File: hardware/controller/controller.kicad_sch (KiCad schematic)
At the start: 26 parts, among them J1 Conn_02x15_Odd_Even, J10 conn_wifi, J11 conn_gpio, J2 Conn_01x20, J3 Conn_01x20, J4 Conn_01x02, J5 conn_vol, J6 conn_bl, J7 conn_br, J8 conn_dsp, J9 conn_i2s_mplx, SW1 RESET, U1 Display_5"_RA8875, U2 TSR_1-2433, U3 TSR_1-2433, U5 TSR_1-2433

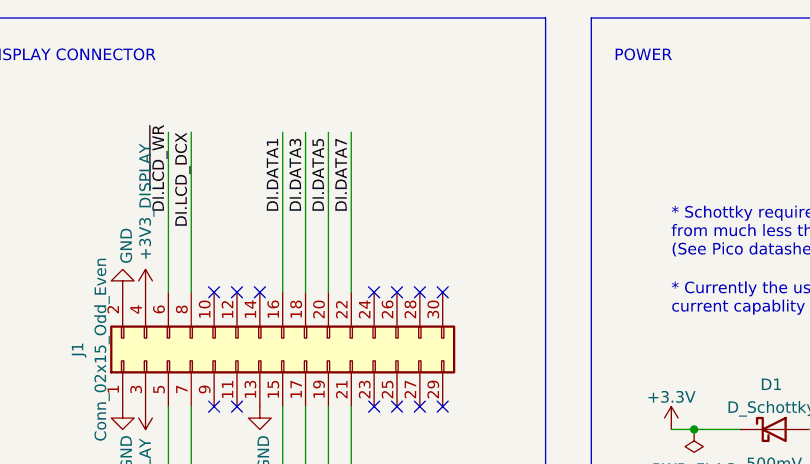
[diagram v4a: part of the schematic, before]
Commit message: Added (temp) backlight control
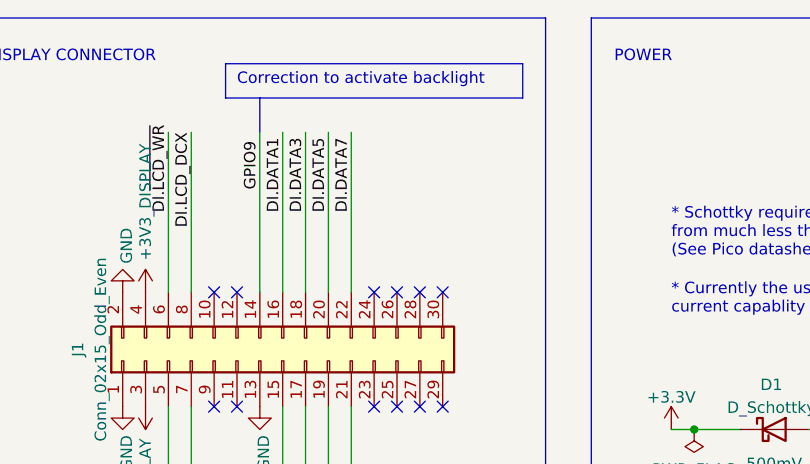
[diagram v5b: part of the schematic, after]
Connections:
- net GPIO9: now also J1.14 (Pin_14)
- no-connect marks 37 -> 36
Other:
- note added: "Correction to activate backlight"
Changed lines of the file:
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@@
   (no_connect (at 100.33 203.2))
   (no_connect (at 100.33 205.74))
-  (no_connect (at 148.59 46.99))
   (no_connect (at 143.51 46.99))
   (no_connect (at 64.77 166.37))
@@
     (stroke (width 0) (type default) (color 0 0 0 0))
   )
+  (polyline (pts (xy 148.59 25.4) (xy 148.59 29.21))
+    (stroke (width 0) (type default) (color 255 0 0 1))
+  )
   (wire (pts (xy 158.75 46.99) (xy 158.75 29.21))
     (stroke (width 0) (type default) (color 0 0 0 0))
@@
     (stroke (width 0) (type default) (color 0 0 0 0))
   )
+  (polyline (pts (xy 144.78 25.4) (xy 177.8 25.4))
+    (stroke (width 0) (type default) (color 255 0 0 1))
+  )
   (polyline (pts (xy 185.42 152.4) (xy 297.18 152.4))
     (stroke (width 0) (type default) (color 0 0 0 0))
@@
     (stroke (width 0) (type default) (color 0 0 0 0))
   )
+  (polyline (pts (xy 177.8 25.4) (xy 177.8 21.59))
+    (stroke (width 0) (type default) (color 255 0 0 1))
+  )
   (wire (pts (xy 345.44 229.87) (xy 345.44 231.14))
     (stroke (width 0) (type default) (color 0 0 0 0))
@@
     (stroke (width 0) (type default) (color 0 0 0 0))
   )
+  (polyline (pts (xy 144.78 21.59) (xy 177.8 21.59))
+    (stroke (width 0) (type default) (color 255 0 0 1))
+  )
   (wire (pts (xy 250.19 134.62) (xy 232.41 134.62))
     (stroke (width 0) (type default) (color 0 0 0 0))
@@
   (wire (pts (xy 317.5 87.63) (xy 346.71 87.63))
     (stroke (width 0) (type default) (color 0 0 0 0))
+  )
+  (polyline (pts (xy 144.78 21.59) (xy 144.78 25.4))
+    (stroke (width 0) (type default) (color 255 0 0 1))
   )
   (polyline (pts (xy 73.66 128.27) (xy 73.66 124.46))
@@
     (stroke (width 0) (type default) (color 0 0 0 0))
   )
+  (wire (pts (xy 148.59 29.21) (xy 148.59 46.99))
+    (stroke (width 0) (type default) (color 0 0 0 0))
+  )
   (wire (pts (xy 67.31 220.98) (xy 67.31 233.68))
     (stroke (width 0) (type default) (color 0 0 0 0))
@@
   )
   (text "Only 8 bit bus used" (at 63.5 88.9 0)
+    (effects (font (size 1.27 1.27)) (justify left bottom))
+  )
+  (text "Correction to activate backlight" (at 146.05 24.13 0)
     (effects (font (size 1.27 1.27)) (justify left bottom))
   )
@@
     (effects (font (size 1.27 1.27)) (justify left bottom))
   )
+  (label "GPIO9" (at 148.59 35.56 90)
+    (effects (font (size 1.27 1.27)) (justify left bottom))
+  )

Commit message: Corrections as of now
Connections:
- net GND: now also J1.23 (Pin_23), J1.24 (Pin_24), J1.25 (Pin_25), J1.26 (Pin_26), J1.27 (Pin_27), J1.28 (Pin_28), J1.29 (Pin_29), J1.30 (Pin_30)
- no-connect marks 36 -> 28
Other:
- note added: "Correction as per suggestion by board manufacturer"
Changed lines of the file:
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@@
   (junction (at 196.85 62.23) (diameter 0) (color 0 0 0 0)
   )
+  (junction (at 168.91 62.23) (diameter 0) (color 0 0 0 0)
+  )
+  (junction (at 166.37 62.23) (diameter 0) (color 0 0 0 0)
+  )
   (junction (at 250.19 62.23) (diameter 0) (color 0 0 0 0)
   )
+  (junction (at 166.37 44.45) (diameter 0) (color 0 0 0 0)
+  )
   (junction (at 328.93 90.17) (diameter 0) (color 0 0 0 0)
   )
   (junction (at 250.19 74.93) (diameter 0) (color 0 0 0 0)
   )
+  (junction (at 163.83 44.45) (diameter 0) (color 0 0 0 0)
+  )
   (junction (at 234.95 62.23) (diameter 0) (color 0 0 0 0)
   )
@@
   (junction (at 337.82 92.71) (diameter 0) (color 0 0 0 0)
   )
+  (junction (at 163.83 62.23) (diameter 0) (color 0 0 0 0)
+  )
+  (junction (at 168.91 44.45) (diameter 0) (color 0 0 0 0)
+  )
   (junction (at 222.25 111.76) (diameter 0) (color 0 0 0 0)
   )
   (junction (at 250.19 35.56) (diameter 0) (color 0 0 0 0)
+  )
+  (junction (at 173.99 62.23) (diameter 0) (color 0 0 0 0)
   )
   (no_connect (at 31.75 64.77))
@@
   (no_connect (at 46.99 185.42))
   (no_connect (at 57.15 185.42))
-  (no_connect (at 166.37 46.99))
-  (no_connect (at 163.83 46.99))
-  (no_connect (at 168.91 46.99))
-  (no_connect (at 161.29 46.99))
-  (no_connect (at 168.91 59.69))
-  (no_connect (at 161.29 59.69))
-  (no_connect (at 166.37 59.69))
-  (no_connect (at 163.83 59.69))
   (no_connect (at 143.51 59.69))
   (no_connect (at 54.61 185.42))
@@
     (stroke (width 0) (type default) (color 0 0 0 0))
   )
+  (wire (pts (xy 168.91 44.45) (xy 168.91 46.99))
+    (stroke (width 0) (type default) (color 0 0 0 0))
+  )
   (wire (pts (xy 82.55 130.81) (xy 82.55 166.37))
     (stroke (width 0) (type default) (color 0 0 0 0))
@@
     (stroke (width 0) (type default) (color 0 0 0 0))
   )
+  (wire (pts (xy 161.29 59.69) (xy 161.29 62.23))
+    (stroke (width 0) (type default) (color 0 0 0 0))
+  )
   (polyline (pts (xy 17.78 232.41) (xy 17.78 222.25))
     (stroke (width 0) (type default) (color 0 0 0 0))
@@
     (stroke (width 0) (type default) (color 0 0 0 0))
   )
+  (polyline (pts (xy 167.64 38.1) (xy 167.64 44.45))
+    (stroke (width 0) (type default) (color 255 0 0 1))
+  )
   (bus (pts (xy 76.2 267.97) (xy 82.55 267.97))
     (stroke (width 0) (type default) (color 0 0 0 0))
@@
   )
   (wire (pts (xy 346.71 161.29) (xy 345.44 161.29))
+    (stroke (width 0) (type default) (color 0 0 0 0))
+  )
+  (wire (pts (xy 168.91 44.45) (xy 173.99 44.45))
     (stroke (width 0) (type default) (color 0 0 0 0))
   )
@@
     (stroke (width 0) (type default) (color 0 0 0 0))
   )
+  (wire (pts (xy 168.91 62.23) (xy 173.99 62.23))
+    (stroke (width 0) (type default) (color 0 0 0 0))
+  )
   (wire (pts (xy 346.71 129.54) (xy 345.44 129.54))
     (stroke (width 0) (type default) (color 0 0 0 0))
@@
     (stroke (width 0) (type default) (color 0 0 0 0))
   )
+  (polyline (pts (xy 161.29 27.94) (xy 177.8 27.94))
+    (stroke (width 0) (type default) (color 255 0 0 1))
+  )
   (wire (pts (xy 146.05 259.08) (xy 144.78 259.08))
     (stroke (width 0) (type default) (color 0 0 0 0))
@@
     (stroke (width 0) (type default) (color 0 0 0 0))
   )
+  (wire (pts (xy 161.29 46.99) (xy 161.29 44.45))
+    (stroke (width 0) (type default) (color 0 0 0 0))
+  )
   (bus (pts (xy 125.73 128.27) (xy 125.73 267.97))
     (stroke (width 0) (type default) (color 0 0 0 0))
@@
   )
   (wire (pts (xy 317.5 92.71) (xy 337.82 92.71))
+    (stroke (width 0) (type default) (color 0 0 0 0))
+  )
+  (wire (pts (xy 166.37 62.23) (xy 168.91 62.23))
     (stroke (width 0) (type default) (color 0 0 0 0))
   )
@@
     (stroke (width 0) (type default) (color 0 0 0 0))
   )
+  (wire (pts (xy 163.83 44.45) (xy 163.83 46.99))
+    (stroke (width 0) (type default) (color 0 0 0 0))
+  )
   (polyline (pts (xy 93.98 119.38) (xy 93.98 124.46))
     (stroke (width 0) (type default) (color 0 0 0 0))
   )
+  (wire (pts (xy 166.37 44.45) (xy 168.91 44.45))
+    (stroke (width 0) (type default) (color 0 0 0 0))
+  )
   (wire (pts (xy 144.78 259.08) (xy 144.78 260.35))
     (stroke (width 0) (type default) (color 0 0 0 0))
@@
     (stroke (width 0) (type default) (color 0 0 0 0))
   )
+  (wire (pts (xy 161.29 62.23) (xy 163.83 62.23))
+    (stroke (width 0) (type default) (color 0 0 0 0))
+  )
   (wire (pts (xy 346.71 127) (xy 345.44 127))
     (stroke (width 0) (type default) (color 0 0 0 0))
@@
     (stroke (width 0) (type default) (color 0 0 0 0))
   )
+  (wire (pts (xy 173.99 44.45) (xy 173.99 62.23))
+    (stroke (width 0) (type default) (color 0 0 0 0))
+  )
   (wire (pts (xy 49.53 181.61) (xy 49.53 185.42))
     (stroke (width 0) (type default) (color 0 0 0 0))
@@
   (wire (pts (xy 317.5 87.63) (xy 346.71 87.63))
     (stroke (width 0) (type default) (color 0 0 0 0))
+  )
+  (polyline (pts (xy 177.8 38.1) (xy 177.8 27.94))
+    (stroke (width 0) (type default) (color 255 0 0 1))
   )
   (polyline (pts (xy 144.78 21.59) (xy 144.78 25.4))
@@
     (stroke (width 0) (type default) (color 0 0 0 0))
   )
+  (wire (pts (xy 173.99 62.23) (xy 173.99 63.5))
+    (stroke (width 0) (type default) (color 0 0 0 0))
+  )
   (wire (pts (xy 153.67 46.99) (xy 153.67 29.21))
     (stroke (width 0) (type default) (color 0 0 0 0))
@@
   )
   (polyline (pts (xy 180.34 274.32) (xy 180.34 111.76))
+    (stroke (width 0) (type default) (color 0 0 0 0))
+  )
+  (wire (pts (xy 168.91 59.69) (xy 168.91 62.23))
+    (stroke (width 0) (type default) (color 0 0 0 0))
+  )
+  (wire (pts (xy 163.83 44.45) (xy 166.37 44.45))
     (stroke (width 0) (type default) (color 0 0 0 0))
   )
@@
     (stroke (width 0) (type default) (color 0 0 0 0))
   )
+  (polyline (pts (xy 161.29 38.1) (xy 177.8 38.1))
+    (stroke (width 0) (type default) (color 255 0 0 1))
+  )
   (wire (pts (xy 67.31 220.98) (xy 67.31 233.68))
     (stroke (width 0) (type default) (color 0 0 0 0))
@@
   )
   (polyline (pts (xy 60.96 25.4) (xy 82.55 25.4))
+    (stroke (width 0) (type default) (color 0 0 0 0))
+  )
+  (wire (pts (xy 163.83 62.23) (xy 166.37 62.23))
     (stroke (width 0) (type default) (color 0 0 0 0))
   )
@@
     (stroke (width 0) (type default) (color 0 0 0 0))
   )
+  (wire (pts (xy 166.37 59.69) (xy 166.37 62.23))
+    (stroke (width 0) (type default) (color 0 0 0 0))
+  )
   (wire (pts (xy 53.34 19.05) (xy 53.34 31.75))
     (stroke (width 0) (type default) (color 0 0 0 0))
@@
     (stroke (width 0) (type default) (color 0 0 0 0))
   )
+  (wire (pts (xy 166.37 44.45) (xy 166.37 46.99))
+    (stroke (width 0) (type default) (color 0 0 0 0))
+  )
   (bus (pts (xy 69.85 128.27) (xy 72.39 128.27))
     (stroke (width 0) (type default) (color 0 0 0 0))
   )
+  (wire (pts (xy 163.83 59.69) (xy 163.83 62.23))
+    (stroke (width 0) (type default) (color 0 0 0 0))
+  )
   (polyline (pts (xy 214.63 205.74) (xy 260.35 205.74))
     (stroke (width 0) (type default) (color 0 0 0 0))
@@
     (stroke (width 0) (type default) (color 0 0 0 0))
   )
+  (wire (pts (xy 161.29 44.45) (xy 163.83 44.45))
+    (stroke (width 0) (type default) (color 0 0 0 0))
+  )
   (bus (pts (xy 77.47 128.27) (xy 82.55 128.27))
     (stroke (width 0) (type default) (color 0 0 0 0))
@@
     (stroke (width 0) (type default) (color 0 0 0 0))
   )
+  (polyline (pts (xy 161.29 27.94) (xy 161.29 38.1))
+    (stroke (width 0) (type default) (color 255 0 0 1))
+  )
   (text "CONNECTORS" (at 309.88 20.32 0)
     (effects (font (size 1.27 1.27)) (justify left bottom))
@@
   )
   (text "Open Source\nHardware" (at 396.24 262.89 0)
+    (effects (font (size 1.27 1.27)) (justify left bottom))
+  )
+  (text "Correction as \nper suggestion \nby board \nmanufacturer"
+    (at 162.56 36.83 0)
     (effects (font (size 1.27 1.27)) (justify left bottom))
   )
@@
     (pin "1")
   )
+  (symbol (lib_id "power:GND") (at 173.99 63.5 0) (unit 1)
+    (in_bom yes) (on_board yes) (fields_autoplaced)
+    (property "Reference" "#PWR?" (id 0) (at 173.99 69.85 0)
+      (effects (font (size 1.27 1.27)) hide)
+    )
+    (property "Value" "GND" (id 1) (at 173.99 67.9434 0))
+    (property "Footprint" "" (id 2) (at 173.99 63.5 0)
+      (effects (font (size 1.27 1.27)) hide)
+    )
+    (property "Datasheet" "" (id 3) (at 173.99 63.5 0)
+      (effects (font (size 1.27 1.27)) hide)
+    )
+    (pin "1")
+  )
   (symbol (lib_id "power:GND") (at 383.54 229.87 0) (unit 1)
     (in_bom yes) (on_board yes) (fields_autoplaced)
@@
       (reference "#PWR0124") (unit 1) (value "+3.3V") (footprint "")
     )
+    (path "/45b32cbe-f349-4537-ac1d-3bcbe169abd8"
+      (reference "#PWR?") (unit 1) (value "GND") (footprint "")
+    )
     (path "/02a22cc8-7c94-420b-8aaa-b9d35bfadbc7"

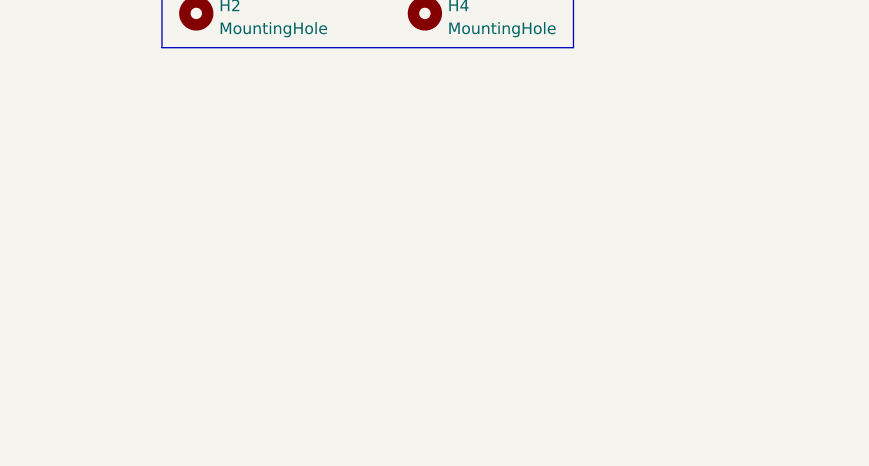
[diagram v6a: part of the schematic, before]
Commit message: Corrections to schematics. WARNING PCB out of date
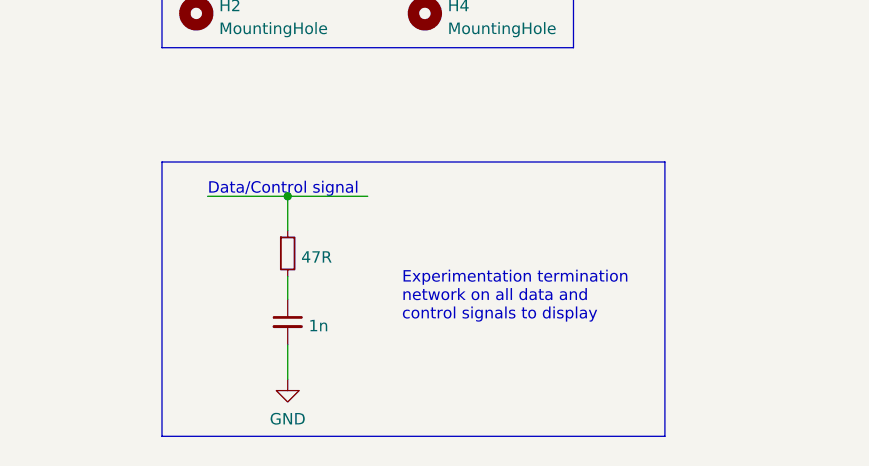
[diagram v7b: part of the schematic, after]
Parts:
- added #C?: 1n, symbol Device:C_Small
- added #R?: 47R, symbol Device:R_Small
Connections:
- net GND: now also #C?.2
- new net: #C?.1, #R?.2
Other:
- note added: "Data/Control signal"
- note added: "Experimentation termination network on all data and control signals to display"
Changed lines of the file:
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@@
   (junction (at 234.95 62.23) (diameter 0) (color 0 0 0 0)
+  )
+  (junction (at 228.6 246.38) (diameter 0) (color 0 0 0 0)
   )
   (junction (at 250.19 100.33) (diameter 0) (color 0 0 0 0)
@@
     (stroke (width 0) (type default) (color 0 0 0 0))
   )
+  (wire (pts (xy 228.6 246.38) (xy 237.49 246.38))
+    (stroke (width 0) (type default) (color 0 0 0 0))
+  )
   (wire (pts (xy 317.5 90.17) (xy 328.93 90.17))
     (stroke (width 0) (type default) (color 0 0 0 0))
@@
     (stroke (width 0) (type default) (color 0 0 0 0))
   )
+  (wire (pts (xy 228.6 262.89) (xy 228.6 266.7))
+    (stroke (width 0) (type default) (color 0 0 0 0))
+  )
   (wire (pts (xy 144.78 259.08) (xy 144.78 260.35))
     (stroke (width 0) (type default) (color 0 0 0 0))
@@
   )
   (wire (pts (xy 85.09 175.26) (xy 85.09 185.42))
+    (stroke (width 0) (type default) (color 0 0 0 0))
+  )
+  (polyline (pts (xy 270.51 242.57) (xy 270.51 273.05))
     (stroke (width 0) (type default) (color 0 0 0 0))
   )
@@
     (stroke (width 0) (type default) (color 255 0 255 1))
   )
+  (polyline (pts (xy 214.63 242.57) (xy 270.51 242.57))
+    (stroke (width 0) (type default) (color 0 0 0 0))
+  )
   (wire (pts (xy 74.93 243.84) (xy 74.93 260.35))
     (stroke (width 0) (type default) (color 0 0 0 0))
@@
     (stroke (width 0) (type default) (color 0 0 0 0))
   )
+  (polyline (pts (xy 270.51 273.05) (xy 214.63 273.05))
+    (stroke (width 0) (type default) (color 0 0 0 0))
+  )
   (wire (pts (xy 58.42 83.82) (xy 58.42 96.52))
     (stroke (width 0) (type default) (color 0 0 0 0))
@@
   )
   (wire (pts (xy 325.12 185.42) (xy 346.71 185.42))
+    (stroke (width 0) (type default) (color 0 0 0 0))
+  )
+  (polyline (pts (xy 214.63 242.57) (xy 214.63 273.05))
     (stroke (width 0) (type default) (color 0 0 0 0))
   )
@@
     (stroke (width 0) (type default) (color 0 0 0 0))
   )
+  (wire (pts (xy 228.6 246.38) (xy 228.6 250.19))
+    (stroke (width 0) (type default) (color 0 0 0 0))
+  )
   (wire (pts (xy 43.18 83.82) (xy 43.18 96.52))
     (stroke (width 0) (type default) (color 0 0 0 0))
@@
     (stroke (width 0) (type default) (color 0 0 0 0))
   )
+  (wire (pts (xy 228.6 255.27) (xy 228.6 257.81))
+    (stroke (width 0) (type default) (color 0 0 0 0))
+  )
   (wire (pts (xy 92.71 156.21) (xy 92.71 166.37))
     (stroke (width 0) (type default) (color 0 0 0 0))
@@
   )
   (polyline (pts (xy 281.94 53.34) (xy 281.94 69.85))
+    (stroke (width 0) (type default) (color 0 0 0 0))
+  )
+  (wire (pts (xy 219.71 246.38) (xy 228.6 246.38))
     (stroke (width 0) (type default) (color 0 0 0 0))
   )
@@
     (effects (font (size 1.27 1.27)) (justify left bottom))
   )
+  (text "Data/Control signal" (at 219.71 246.38 0)
+    (effects (font (size 1.27 1.27)) (justify left bottom))
+  )
   (text "Open Source\nHardware" (at 396.24 262.89 0)
     (effects (font (size 1.27 1.27)) (justify left bottom))
@@
   )
   (text "PICO MCU\n" (at 19.05 115.57 0)
+    (effects (font (size 1.27 1.27)) (justify left bottom))
+  )
+  (text "Experimentation termination\nnetwork on all data and \ncontrol signals to display"
+    (at 241.3 260.35 0)
     (effects (font (size 1.27 1.27)) (justify left bottom))
   )
@@
     (pin "1")
   )
+  (symbol (lib_id "power:GND") (at 228.6 266.7 0) (unit 1)
+    (in_bom yes) (on_board yes) (fields_autoplaced)
+    (property "Reference" "#PWR?" (id 0) (at 228.6 273.05 0)
+      (effects (font (size 1.27 1.27)) hide)
+    )
+    (property "Value" "GND" (id 1) (at 228.6 271.1434 0))
+    (property "Footprint" "" (id 2) (at 228.6 266.7 0)
+      (effects (font (size 1.27 1.27)) hide)
+    )
+    (property "Datasheet" "" (id 3) (at 228.6 266.7 0)
+      (effects (font (size 1.27 1.27)) hide)
+    )
+    (pin "1")
+  )
   (symbol (lib_id "power:+3.3V") (at 194.31 62.23 0) (unit 1)
     (in_bom yes) (on_board yes) (fields_autoplaced)
@@
     )
     (pin "1")
+  )
+  (symbol (lib_id "Device:C_Small") (at 228.6 260.35 0) (unit 1)
+    (in_bom yes) (on_board yes) (fields_autoplaced)
+    (property "Reference" "#C?" (id 0) (at 230.9241 259.5216 0)
+      (effects (font (size 1.27 1.27)) (justify left) hide)
+    )
+    (property "Value" "1n" (id 1) (at 230.9241 260.7901 0)
+      (effects (font (size 1.27 1.27)) (justify left))
+    )
+    (property "Footprint" "" (id 2) (at 228.6 260.35 0)
+      (effects (font (size 1.27 1.27)) hide)
+    )
+    (property "Datasheet" "~" (id 3) (at 228.6 260.35 0)
+      (effects (font (size 1.27 1.27)) hide)
+    )
+    (pin "1")
+    (pin "2")
   )
   (symbol (lib_id "project:+3V3_DISPLAY") (at 31.75 44.45 90) (unit 1)
@@
     )
     (pin "1")
+  )
+  (symbol (lib_id "Device:R_Small") (at 228.6 252.73 0) (unit 1)
+    (in_bom yes) (on_board yes) (fields_autoplaced)
+    (property "Reference" "#R?" (id 0) (at 230.0986 251.8953 0)
+      (effects (font (size 1.27 1.27)) (justify left) hide)
+    )
+    (property "Value" "47R" (id 1) (at 230.0986 253.1638 0)
+      (effects (font (size 1.27 1.27)) (justify left))
+    )
+    (property "Footprint" "" (id 2) (at 228.6 252.73 0)
+      (effects (font (size 1.27 1.27)) hide)
+    )
+    (property "Datasheet" "~" (id 3) (at 228.6 252.73 0)
+      (effects (font (size 1.27 1.27)) hide)
+    )
+    (pin "1")
+    (pin "2")
   )
   (symbol (lib_id "project:Display_5{dblquote}_RA8875") (at 60.96 55.88 0) (unit 1)
@@
   )
   (symbol_instances
+    (path "/af1102d8-3fca-4528-ae86-8b51184d5f5e"
+      (reference "#C?") (unit 1) (value "1n") (footprint "")
+    )
     (path "/996a8dc6-561a-443a-8843-e688e3bd2e77"
       (reference "#FLG01") (unit 1) (value "PWR_FLAG") (footprint "")
@@
       (reference "#PWR?") (unit 1) (value "GND") (footprint "")
     )
+    (path "/7ed4ef6f-5219-410b-a78f-a27322c389cf"
+      (reference "#PWR?") (unit 1) (value "GND") (footprint "")
+    )
+    (path "/f482f350-a5ad-43b8-9ec2-07fb6ee67689"
+      (reference "#R?") (unit 1) (value "47R") (footprint "")
+    )
     (path "/02a22cc8-7c94-420b-8aaa-b9d35bfadbc7"
